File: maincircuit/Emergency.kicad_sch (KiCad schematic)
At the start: 9 parts, among them J5 Conn_01x02_Pin, Q1 Q_NMOS, Q2 Q_NMOS, U1 TLP250

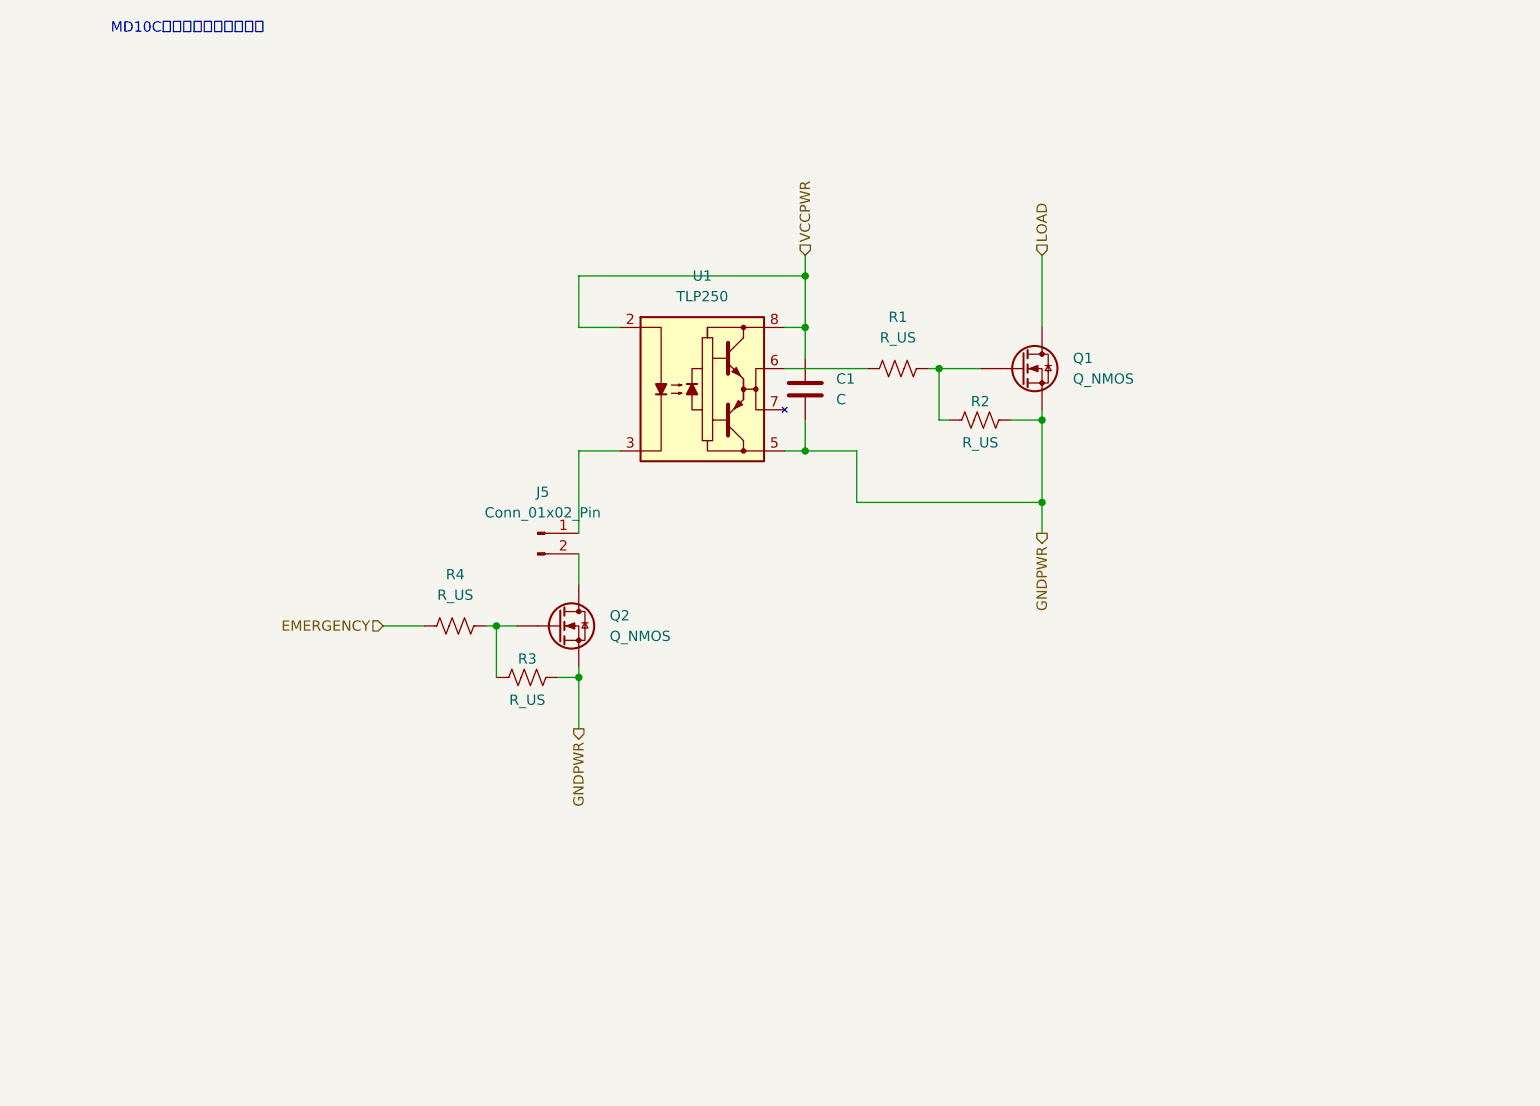
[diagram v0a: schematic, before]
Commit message: add: 07/13進捗分(主にcontrol回路)
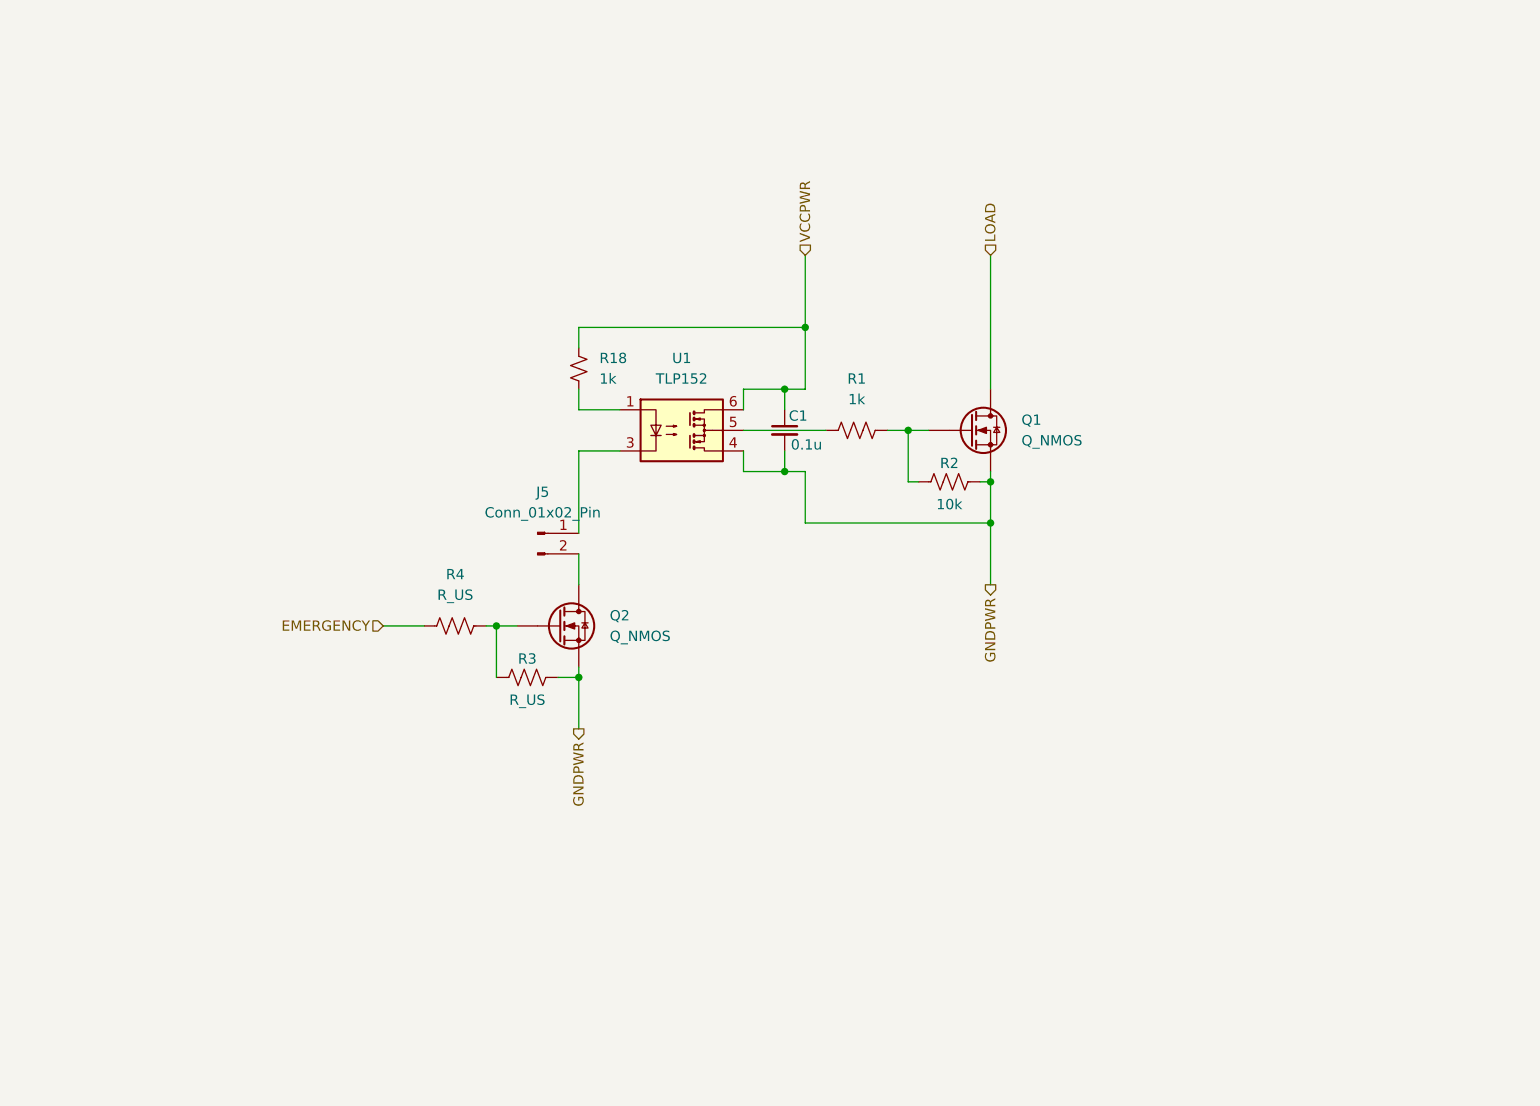
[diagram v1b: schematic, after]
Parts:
- removed C1: C, symbol Device:C
- removed U1: TLP250, Package_DIP:DIP-8_W7.62mm, symbol Driver_FET:TLP250
- added C1: 0.1u, Capacitor_SMD:C_0603_1608Metric_Pad1.08x0.95mm_HandSolder, symbol Device:C_Small
- added R18: 1k, symbol Device:R_Small_US
- added U1: TLP152, Package_SO:SO-5-6_4.55x3.7mm_P1.27mm, symbol Library:TLP152
- R1: value R_US -> 1k
- R2: value R_US -> 10k
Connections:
- net GNDPWR: now also C1.2, U1.4
- net VCCPWR: now also C1.1, R18.1, U1.6
- net at R1.1: now also U1.5
- net at J5.1 (Pin_1): now also U1.3
- new net: R18.2, U1.1
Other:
- note removed: "MD10Cは（おそらく）非絶縁"
- moved on the sheet: Q1, R1, R2

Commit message: [add]ControlCircuit完成
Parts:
- removed C1: 0.1u, Capacitor_SMD:C_0603_1608Metric_Pad1.08x0.95mm_HandSolder, symbol Device:C_Small
- removed J5: Conn_01x02_Pin, symbol Connector:Conn_01x02_Pin
- removed Q2: Q_NMOS, symbol Device:Q_NMOS
- removed R1: 1k, symbol Device:R_US
- removed R18: 1k, symbol Device:R_Small_US
- removed R2: 10k, symbol Device:R_US
- removed R3, R4: R_US, symbol Device:R_US
- removed U1: TLP152, Package_SO:SO-5-6_4.55x3.7mm_P1.27mm, symbol Library:TLP152
- added D1: D, symbol Device:D
- added K1: G2R-1-E, Library:G2R-1-E, symbol Library:G2R-1-E
- added R1: 1k, symbol Device:R_Small_US
- added R2: 10k, symbol Device:R_Small_US
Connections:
- net EMERGENCY: now also R1.1
- net GNDPWR: now also K1.11, R2.2
- net LOAD: now also K1.14; no longer Q1.D
- net VCCPWR: now also D1.1 (K), K1.A1
- net at Q1.G: now also R1.2, R2.1
- new net: D1.2 (A), K1.A2, Q1.D

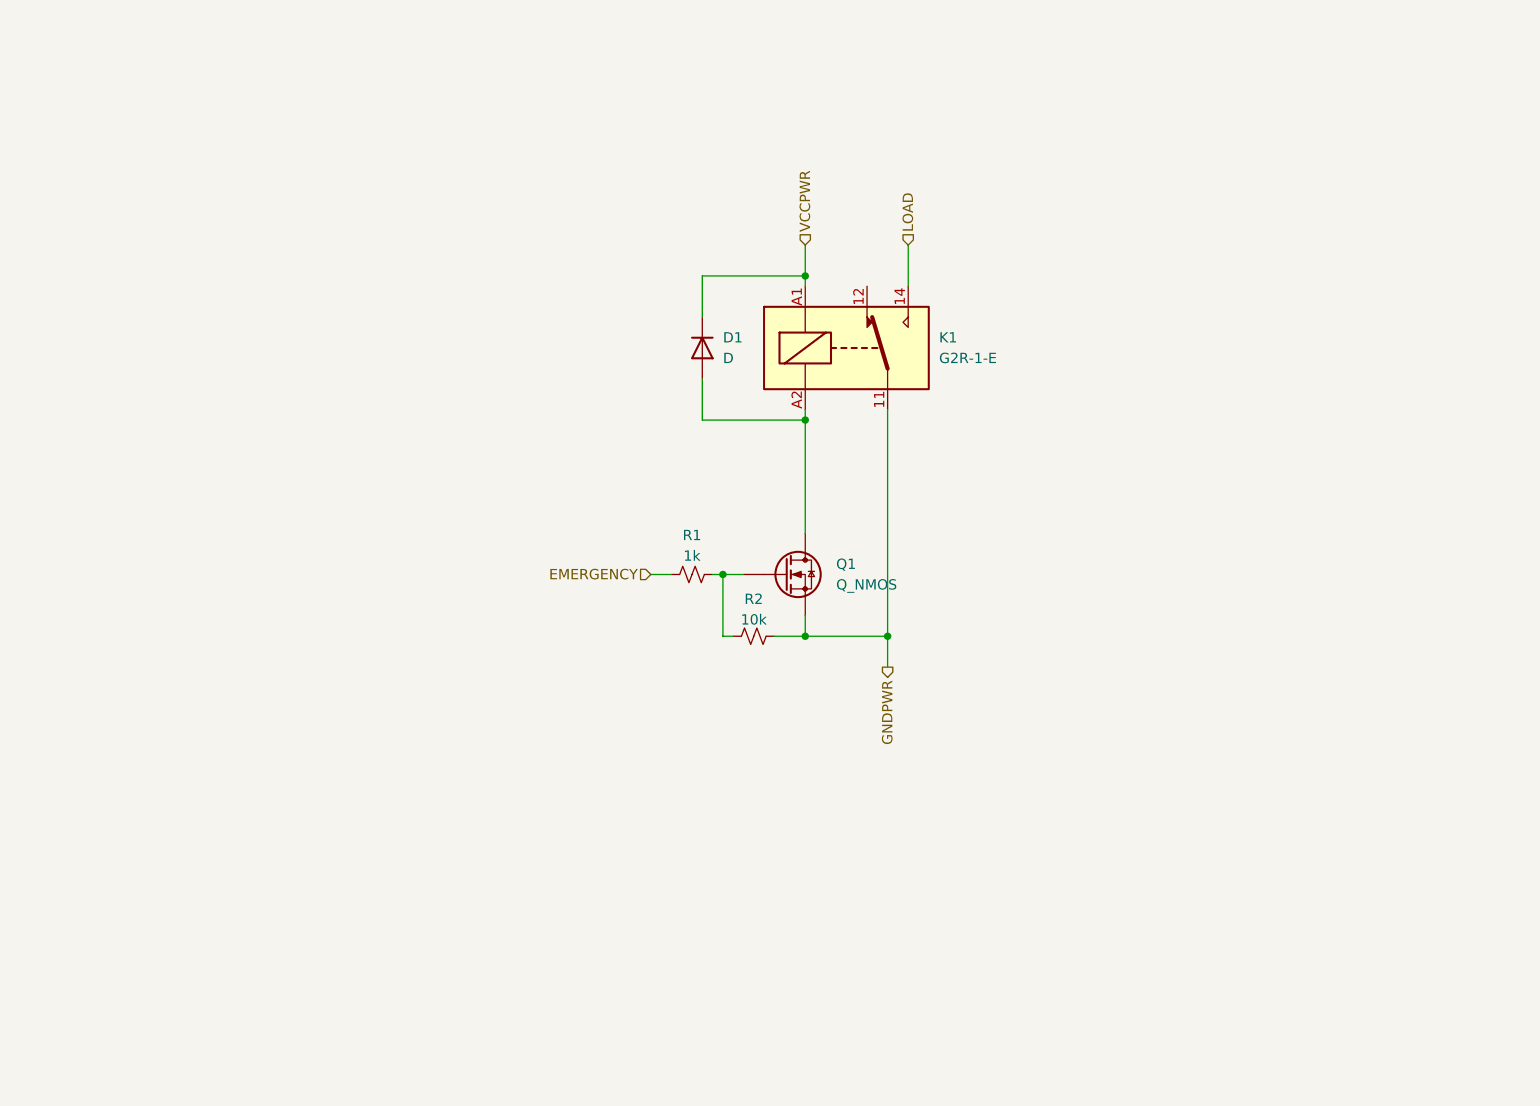
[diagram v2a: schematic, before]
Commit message: add: ver1.0の基板データの完成
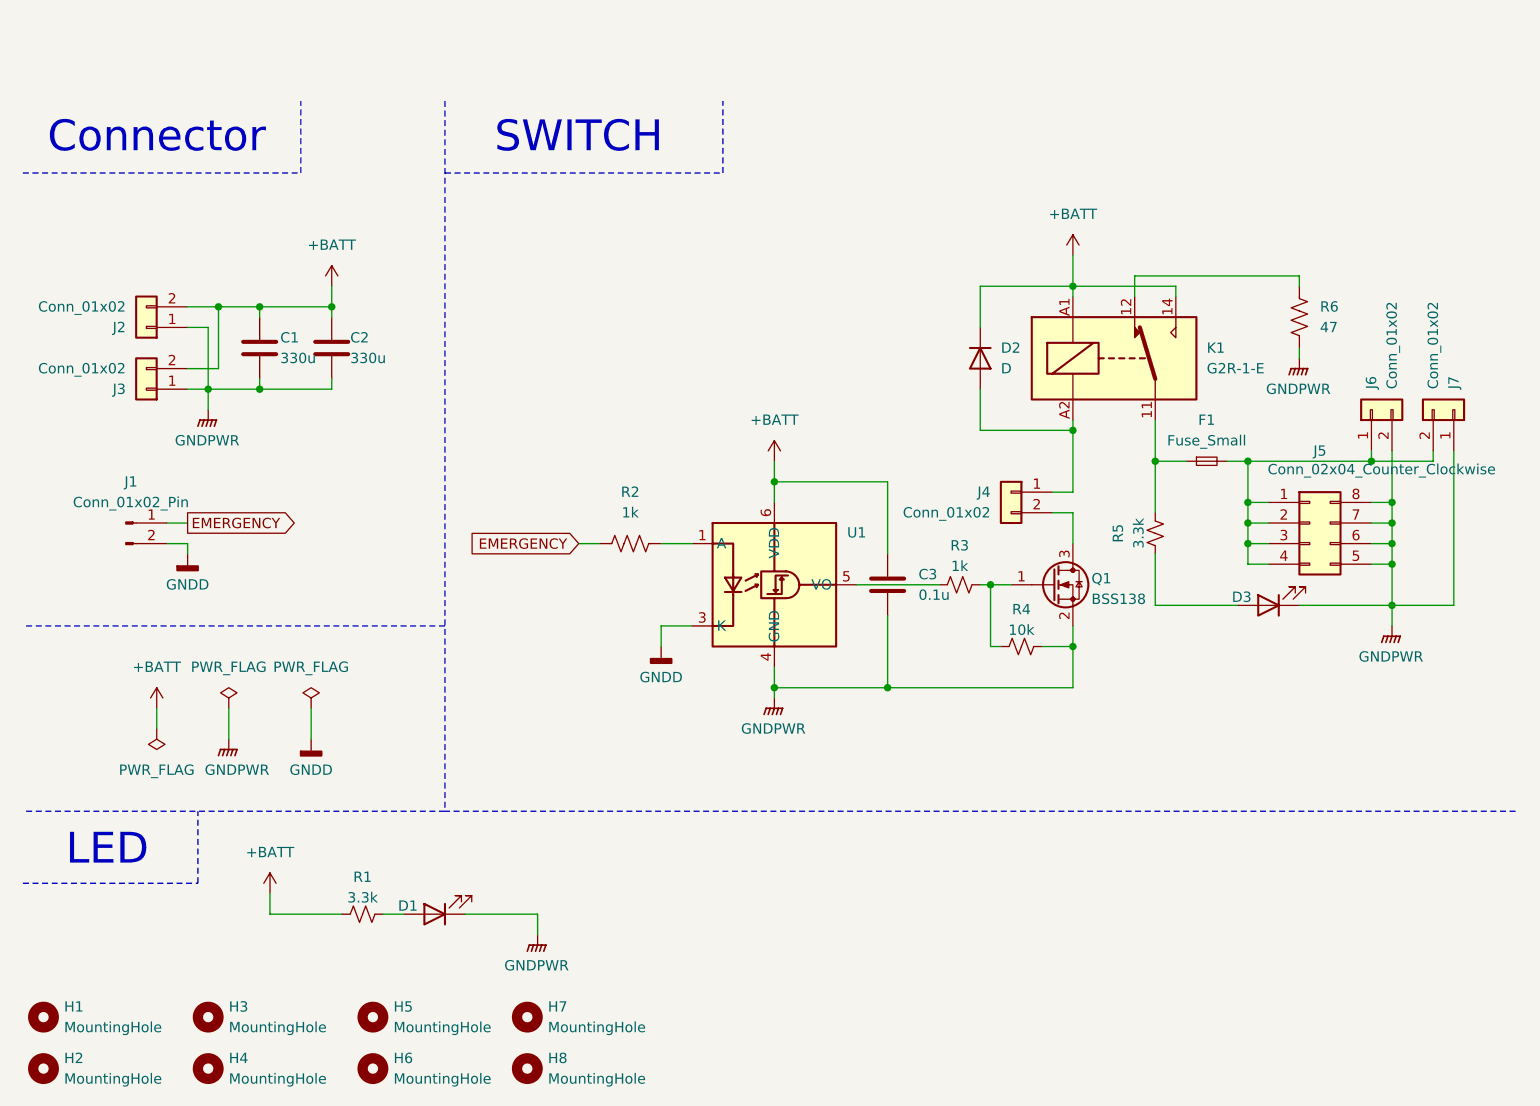
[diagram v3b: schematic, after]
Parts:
- removed D1: D, symbol Device:D
- removed Q1: Q_NMOS, symbol Device:Q_NMOS
- added C1, C2: 330u, Capacitor_SMD:CP_Elec_10x10, symbol Device:C
- added C3: 0.1u, Capacitor_SMD:C_0603_1608Metric_Pad1.08x0.95mm_HandSolder, symbol Device:C
- added D1, D3: LED, LED_SMD:LED_0603_1608Metric, symbol Device:LED
- added D2: D, Diode_THT:D_DO-201AD_P15.24mm_Horizontal, symbol Device:D
- added F1: Fuse_Small, Library:FUC-04, symbol Device:Fuse_Small
- added H1, H2, H3, H4, H5, H6, H7, H8: MountingHole, MountingHole:MountingHole_3.2mm_M3, symbol Mechanical:MountingHole
- added J1: Conn_01x02_Pin, Connector_PinSocket_2.54mm:PinSocket_1x02_P2.54mm_Vertical, symbol Connector:Conn_01x02_Pin
- added J2: Conn_01x02, Connector_AMASS:AMASS_XT60PW-M_1x02_P7.20mm_Horizontal, symbol Connector_Generic:Conn_01x02
- added J3, J7: Conn_01x02, Connector_AMASS:AMASS_XT60PW-F_1x02_P7.20mm_Horizontal, symbol Connector_Generic:Conn_01x02
- added J4, J6: Conn_01x02, Connector_JST:JST_XH_B2B-XH-A_1x02_P2.50mm_Vertical, symbol Connector_Generic:Conn_01x02
- added J5: Conn_02x04_Counter_Clockwise, Connector_PinSocket_2.54mm:PinSocket_2x04_P2.54mm_Vertical, symbol Connector_Generic:Conn_02x04_Counter_Clockwise
- added Q1: BSS138, Package_TO_SOT_SMD:SOT-23, symbol Transistor_FET:BSS138
- added R1, R5: 3.3k, Resistor_SMD:R_0603_1608Metric_Pad0.98x0.95mm_HandSolder, symbol Device:R_Small_US
- added R2: 1k, Resistor_SMD:R_0603_1608Metric_Pad0.98x0.95mm_HandSolder, symbol Device:R_US
- added R6: 47, Resistor_THT:R_Axial_DIN0614_L14.3mm_D5.7mm_P20.32mm_Horizontal, symbol Device:R_US
- added U1: ~, Package_SO:SO-5-6_4.55x3.7mm_P1.27mm, symbol Library:TLP2348
- R3: renamed from R1; footprint (none) -> Resistor_SMD:R_0603_1608Metric_Pad0.98x0.95mm_HandSolder
- R4: renamed from R2; footprint (none) -> Resistor_SMD:R_0603_1608Metric_Pad0.98x0.95mm_HandSolder
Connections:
- net VCCPWR is gone; now on net +BATT: K1.A1
- net EMERGENCY: now also J1.1 (Pin_1), R2.1; no longer R3.1
- net GNDPWR: now also C1.2, C2.2, C3.2, D1.1 (K), D3.1 (K), J2.1 (Pin_1), J3.1 (Pin_1), J5.5 (Pin_5), J5.6 (Pin_6), J5.7 (Pin_7), J5.8 (Pin_8), J6.2 (Pin_2), J7.1 (Pin_1), Q1.2 (S), R6.2, U1.4 (GND); no longer K1.11
- net at K1.12: now also R6.1
- net at K1.A2: now also D2.2 (A), J4.1 (Pin_1)
- net at R3.2, R4.1: now also Q1.1 (G)
- net LOAD renamed +BATT
- net +BATT: now also C1.1, C2.1, C3.1, D2.1 (K), J2.2 (Pin_2), J3.2 (Pin_2), R1.1, U1.6 (VDD)
- new net: D1.2 (A), R1.2
- new net: D3.2 (A), R5.1
- new net: F1.1, K1.11, R5.2
- new net: F1.2, J5.1 (Pin_1), J5.2 (Pin_2), J5.3 (Pin_3), J5.4 (Pin_4), J6.1 (Pin_1), J7.2 (Pin_2)
- new net: J4.2 (Pin_2), Q1.3 (D)
- new net: R3.1, U1.5 (VO)
- new net: R2.2, U1.1 (A)
- new net GNDD: J1.2 (Pin_2), U1.3 (K)
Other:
- note added: "Connector"
- note added: "LED"
- note added: "SWITCH"
- moved on the sheet: K1, R3, R4
